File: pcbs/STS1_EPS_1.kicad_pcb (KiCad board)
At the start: 4 copper layers, 81 x 85 mm, 157 parts, among them J1 Inter-EPS, J2 Panel Y+, J4 Panel Y-, J5 Panel X+, J6 Panel X-, J7 Panel Z-, Q1 SI7135DP-T1-GE3, Q2 SI7135DP-T1-GE3, Q3 SI7135DP-T1-GE3, Q4 2N7002, Q5 2N7002, Q6 2N7002, Q7 2N7002, U1 LTC4020EUHFPBF, U10 MAX11632EEGT, U11 INA180A4, U12 BD50GA5WEFJ, U13 TPS259472ARPW, U14 LM334M, U15 LM334M, U16 LM334M, U17 LM334M, U18 LM334M, U19 TPS259472ARPW, U2 SI7272DP-T1-GE3, U20 TPS259472ARPW, U21 TPS259472ARPW, U22 TPS259472ARPW, U23 TPS259472ARPW, U24 TPS259472ARPW, U27 LTC4451AV#TRMPBF, U28 LTC4451AV#TRMPBF, U3 SI7272DP-T1-GE3, U4 TPS259472ARPW, U5 MAX11632EEGT, U6 MAX11632EEGT, U7 MAX11632EEGT, U8 MAX11632EEGT, U9 MAX11632EEGT

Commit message: Changed connectors of STS_EPS_1 ...again.
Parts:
- CSBI_1, CSBI_2: value ESQT-125-02-F-D-800 -> ESQT-125-02-F-D-560
- R24, R52: value 87k5 -> 86k6
- R7: value 500k -> 499k
- R9: value 166k -> 169k
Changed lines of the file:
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@@
       (effects (font (size 1 1) (thickness 0.15)))
     )
-    (fp_text value "ESQT-125-02-F-D-800" (at 1 50.06) (layer "F.Fab") hide
+    (fp_text value "ESQT-125-02-F-D-560" (at 1 50.06) (layer "F.Fab") hide
       (effects (font (size 1 1) (thickness 0.15)))
     )
@@
     (pad "50" thru_hole oval locked (at 2 48) (size 1.35 1.35) (drill 0.8) (layers *.Cu *.Mask)
       (net 1 "GND") (pinfunction "Pin_50") (pintype "passive"))
-    (model ":STS_Connector:ESQT-125-02-M-D-640.stp"
-      (offset (xyz 1 -24 10))
+    (model ":STS_Connector:ESQT-125-02-M-D-560.stp"
+      (offset (xyz 1 -24 7.9))
       (scale (xyz 1 1 1))
       (rotate (xyz -90 0 90))
@@
       (effects (font (size 1 1) (thickness 0.15)))
     )
-    (fp_text value "ESQT-125-02-F-D-800" (at 1 50.06) (layer "F.Fab") hide
+    (fp_text value "ESQT-125-02-F-D-560" (at 1 50.06) (layer "F.Fab") hide
       (effects (font (size 1 1) (thickness 0.15)))
     )
@@
     (pad "50" thru_hole oval locked (at 2 48) (size 1.35 1.35) (drill 0.8) (layers *.Cu *.Mask)
       (net 1 "GND") (pinfunction "Pin_50") (pintype "passive"))
-    (model ":STS_Connector:ESQT-125-02-M-D-640.stp"
-      (offset (xyz 1 -24 10))
+    (model ":STS_Connector:ESQT-125-02-M-D-560.stp"
+      (offset (xyz 1 -24 7.9))
       (scale (xyz 1 1 1))
       (rotate (xyz -90 0 90))
@@
       (effects (font (size 1 1) (thickness 0.15)))
     )
-    (fp_text value "87k5" (at 0 1.65) (layer "F.Fab")
+    (fp_text value "86k6" (at 0 1.65) (layer "F.Fab")
       (effects (font (size 1 1) (thickness 0.15)))
     )
@@
     (descr "Through hole straight pin header, 2x11, 2.00mm pitch, double rows")
     (tags "Through hole pin header THT 2x11 2.00mm double row")
-    (property "Part#" "ESQT-107-02-F-D-800")
+    (property "Part#" "ESQT-111-02-F-D-560")
     (property "Sheetfile" "STS1_EPS_1.kicad_sch")
     (property "Sheetname" "")
@@
     (pad "22" thru_hole oval locked (at 2 20 90) (size 1.35 1.35) (drill 0.8) (layers *.Cu *.Mask)
       (net 182 "/MPPT_SUM") (pinfunction "Pin_22") (pintype "passive"))
-    (model ":STS_Connector:ESQT-111-02-F-D-640.stp"
-      (offset (xyz 1 -10 10))
+    (model ":STS_Connector:ESQT-111-02-M-D-560.stp"
+      (offset (xyz 1 -10 7.9))
       (scale (xyz 1 1 1))
-      (rotate (xyz 90 180 90))
+      (rotate (xyz -90 0 90))
     )
   )
@@
       (effects (font (size 1 1) (thickness 0.15)))
     )
-    (fp_text value "87k5" (at 0 1.65 90) (layer "F.Fab")
+    (fp_text value "86k6" (at 0 1.65 90) (layer "F.Fab")
       (effects (font (size 1 1) (thickness 0.15)))
     )
@@
       (effects (font (size 1 1) (thickness 0.15)) (justify mirror))
     )
-    (fp_text value "500k" (at 0 -1.65) (layer "B.Fab")
+    (fp_text value "499k" (at 0 -1.65) (layer "B.Fab")
       (effects (font (size 1 1) (thickness 0.15)) (justify mirror))
     )
@@
       (effects (font (size 1 1) (thickness 0.15)) (justify mirror))
     )
-    (fp_text value "166k" (at 0 -1.65 90) (layer "B.Fab")
+    (fp_text value "169k" (at 0 -1.65 90) (layer "B.Fab")
       (effects (font (size 1 1) (thickness 0.15)) (justify mirror))
     )

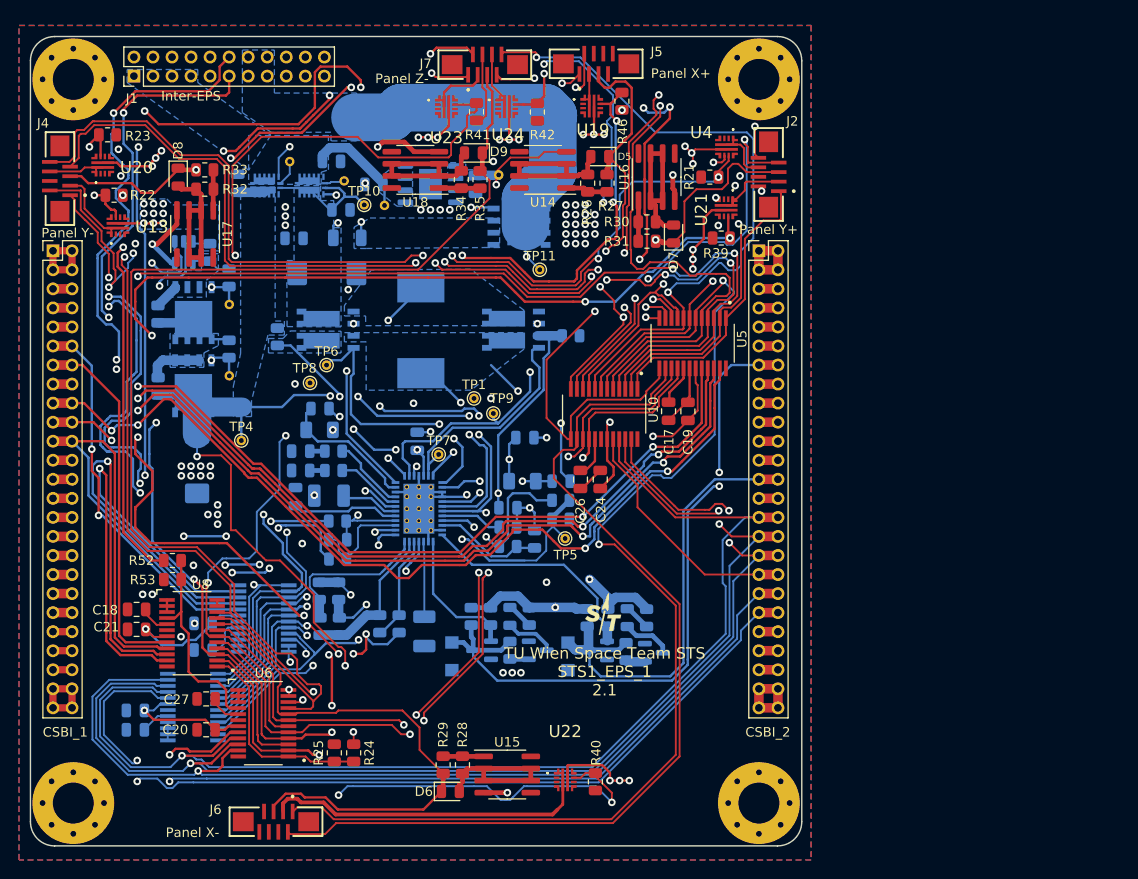
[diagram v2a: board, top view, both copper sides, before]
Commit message: Adjusted CSBI so it conforms to the new version of it.
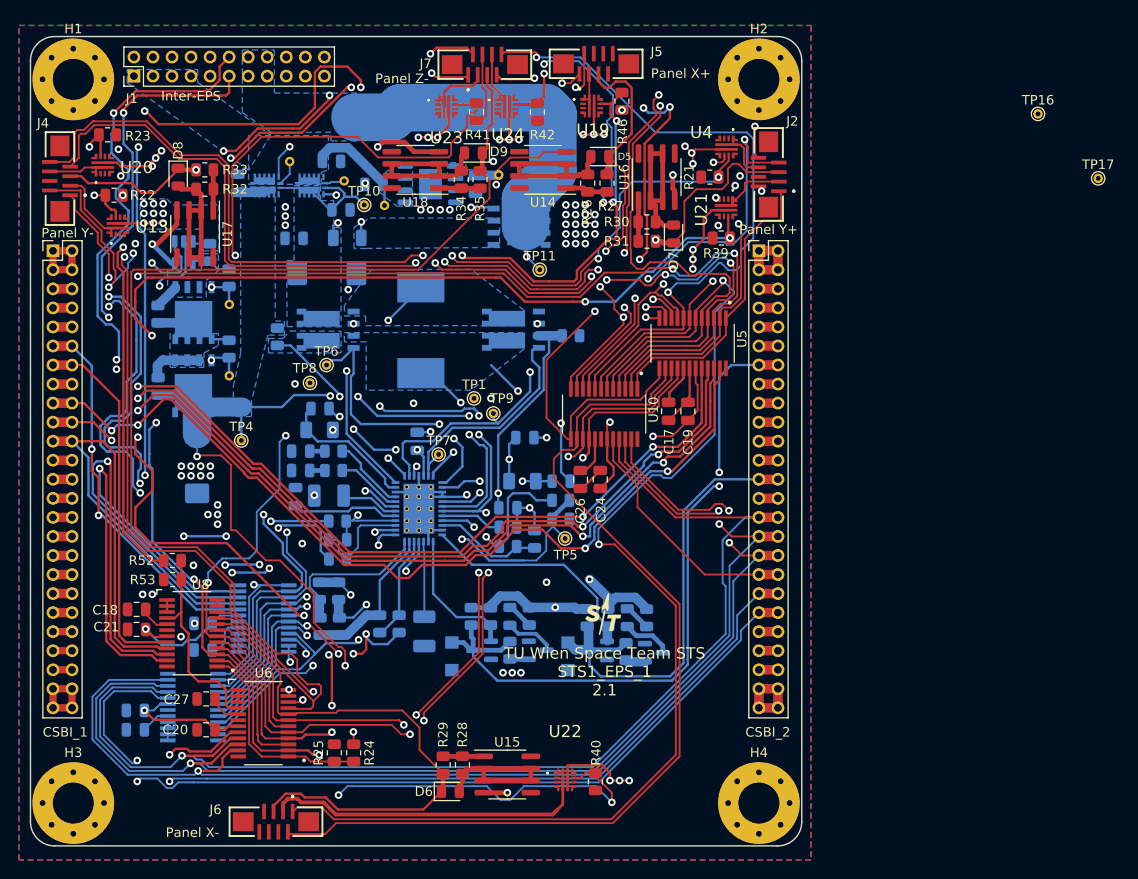
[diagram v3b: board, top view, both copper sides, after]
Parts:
- added TP16: TestPoint, TestPoint:TestPoint_THTPad_D1.0mm_Drill0.5mm, F.Cu at (171.5, 89.5)
- added TP17: TestPoint, TestPoint:TestPoint_THTPad_D1.0mm_Drill0.5mm, F.Cu at (177.8, 96.3)
- H1, H2, H3, H4: value MountingHole -> MountingHole_Pad
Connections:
- CSBI_2 pad 10: GND -> Net-(CSBI_2-Pin_10)
- CSBI_2 pad 9: GND -> Net-(CSBI_2-Pin_10)
- H1 pad 1: (no net) -> GND
- H2 pad 1: (no net) -> GND
- H3 pad 1: (no net) -> GND
- H4 pad 1: (no net) -> GND
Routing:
- net Net-(CSBI_2-Pin_10): track 0.00 -> 2.00 mm
- net GND: track 108.2 -> 106.2 mm
